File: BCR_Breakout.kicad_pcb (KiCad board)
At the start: 2 copper layers, 21.7 x 13.2 mm, 2 parts, among them CN1 DB9_Female, CN2 UE27AC54100

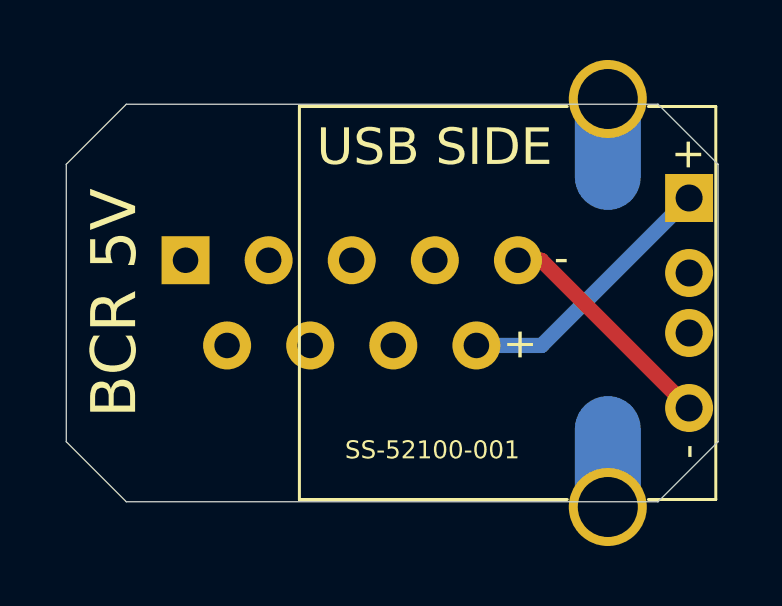
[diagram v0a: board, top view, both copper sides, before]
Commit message: Add BCR_Breakout. Rename repo to BCR_Breakout.
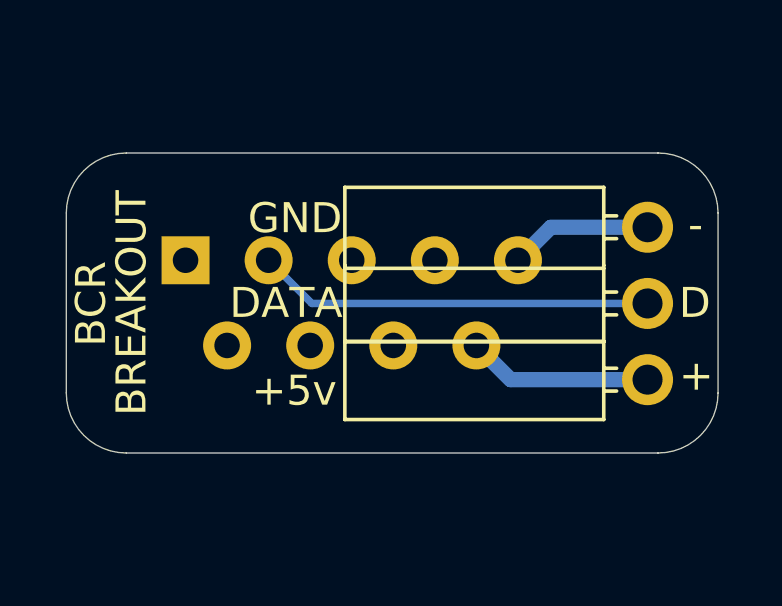
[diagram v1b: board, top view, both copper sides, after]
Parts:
- CN2: footprint 0_LOCAL:USB_A_Female_UE27AC54100_cut -> 0_LOCAL:Socket_Strip_Angled_1x03_Pitch2.54mm
- moved CN2 2.85 mm to (136.9, 93.2), turned to 0 degrees
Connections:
- CN1 pad 2: (no net) -> /RXD
- CN1 pad 7: (no net) -> /GND
- CN2 pad 1: /+5V -> /GND
- CN2 pad 2: (no net) -> /RXD
- CN2 pad 3: (no net) -> /+5V
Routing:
- net /RXD: track 0.00 -> 13.2 mm
- net /GND: track 7.75 -> 4.78 mm
- net /+5V: track 9.13 -> 6.18 mm
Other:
- board size 21.7 x 13.2 mm -> 21.7 x 10 mm
- board text added: "+5v"
- board text added: "BCR"
- board text added: "BREAKOUT"
- board text added: "D"
- board text added: "DATA"
- board text added: "GND"
- board text removed: "BCR 5V"
- board text removed: "BCR to USB 5v"
- board text removed: "SS-52100-001"
- board text removed: "USB SIDE"

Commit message: change metal db9 to plastic
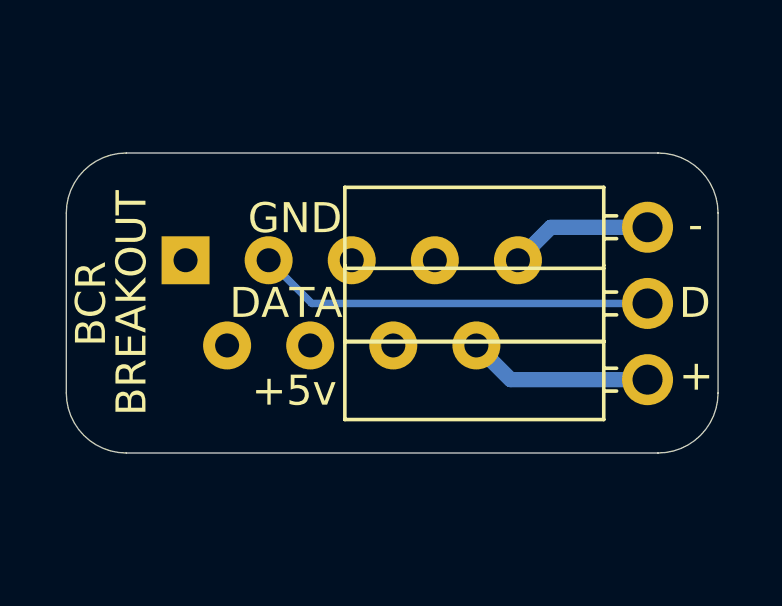
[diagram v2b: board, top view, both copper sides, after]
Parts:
- CN1: footprint 0_LOCAL:DSUB-9_Female_Vertical_metal -> 0_LOCAL:TE-5207826_cut
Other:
- board text added: "TE 5207826"
- board text removed: "A-DF 09 PP/Z"

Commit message: db9 pin 7 is the real GND, not pin 5
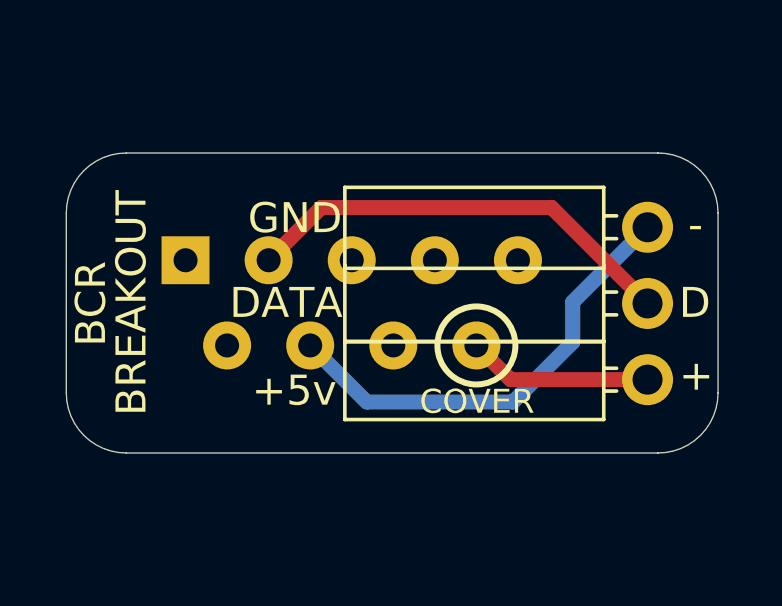
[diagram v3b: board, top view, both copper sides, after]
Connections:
- CN1 pad 5: /GND -> (no net)
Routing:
- net /GND: track 4.78 -> 15.2 mm
- net /RXD: track 13.2 -> 14.7 mm
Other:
- net class Default: clearance 0.2 -> 0.16; trace_width 0.25 -> 0.16; via_dia 0.8 -> 0.42; via_drill 0.4 -> 0.26
- rule trace_clearance: 0.2 -> 0.16
- rule trace_min: 0.2 -> 0.16
- rule via_min_drill: 0.3 -> 0.26
- rule via_min_size: 0.4 -> 0.42
- board text added: "COVER"
